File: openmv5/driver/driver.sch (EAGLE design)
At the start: 83 parts, among them IC1 TPS613222ADBVR, IC2 AP64060WU-7, IC3 LM321LVIDCKR, IC4 74LVC1G07GW,125, IC5 DRV8876RGTR, IC6 DRV8876RGTR, J1 OPENMV5-TOP, J2 1771088, Q1 BUK6D120-60PX, U1 74LVC1G17SE-7

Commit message: Finish up driver shield
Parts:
- C16, C17: value EEV226M050S9GAA -> EMZR500ARA101MF80G; device EEV226M050S9GAA:EEV226M050S9GAA -> EMZR500ARA101MF80G:EMZR500ARA101MF80G; MPN EEV226M050S9GAA -> EMZR500ARA101MF80G
- R10: MPN CRCW04021K00FKEDC -> AC0402FR-1310KL
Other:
- note added: "* PMODE States: ---Low--- (Speed/Direction Mode) P7 = PWM P7=0% -> Out1,Out2=L,L (motor break) P7=1%-100% (below) P0 = Direction P0=L -> Out1,Out2=L,H (motor reverse) P0=H -> Out1,Out2=H,L (motor forward) ---High--- (H-Bridge Mode - Can be PWMed) P0,P8=L,L -> Out1,Out2=Hi-Z,Hi-Z (motor coast) P0,P8=L,H -> Out1,Out2=H,L (motor forward) P0,P8=H,L -> Out1,Out2=L,H (motor reverse) P0,P8=H,H -> Out1,O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"
- note added: "* PMODE States: ---Low--- (Speed/Direction Mode) P8 = PWM P8=0% -> Out3,Out4=L,L (motor break) P8=1%-100% (below) P12 = Direction P12=L -> Out3,Out4=L,H (motor reverse) P12=H -> Out3,Out4=H,L (motor forward) ---High--- (H-Bridge Mode - Can be PWMed) P12,P8=L,L -> Out3,Out4=Hi-Z,Hi-Z (motor coast) P12,P8=L,H -> Out3,Out4=H,L (motor forward) P12,P8=H,L -> Out3,Out4=L,H (motor reverse) P12,P8=H,H ->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"
- moved on the sheet: C13, C15, C17, C20, C21, D11, D13, IC6, JP11, R13, R15

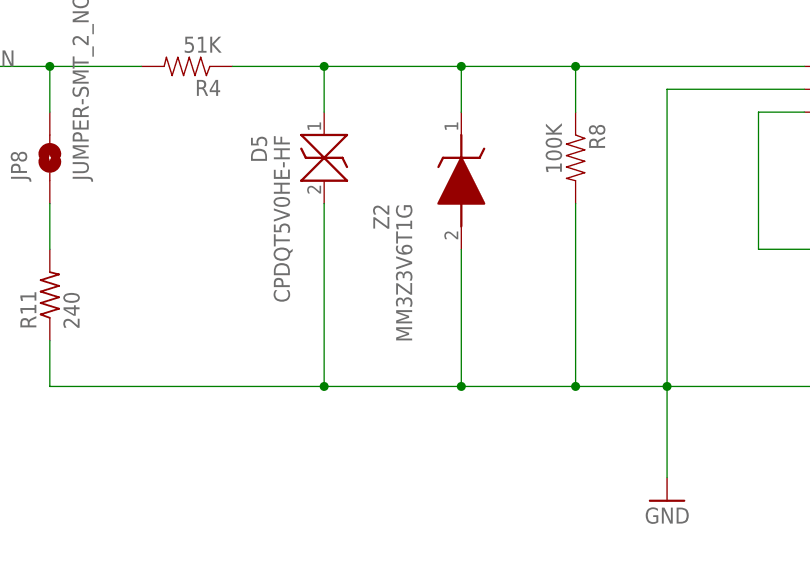
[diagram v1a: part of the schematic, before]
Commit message: Remove zener diode from ADC circuit
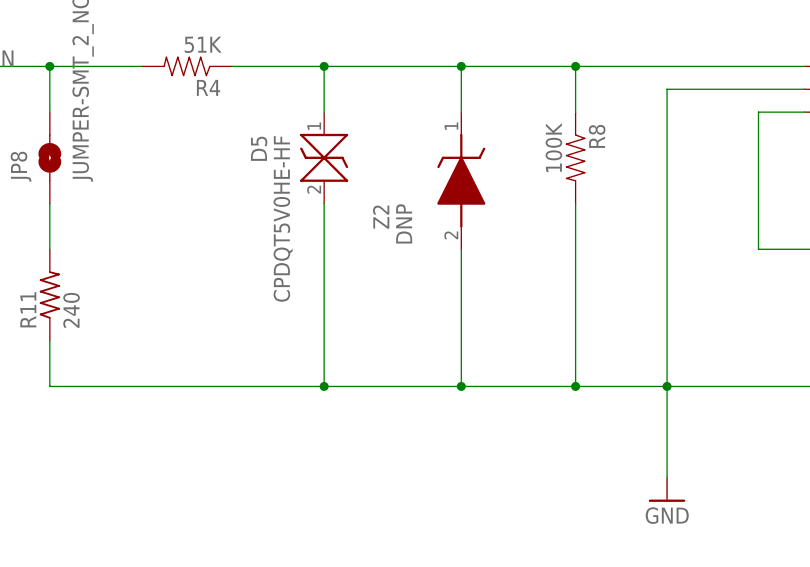
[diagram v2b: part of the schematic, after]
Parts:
- Z2: value MM3Z3V6T1G -> DNP; POPULATE (none) -> 0
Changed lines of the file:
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@@
 </part>
 <part name="GND7" library="sfe" deviceset="GND" device=""/>
-<part name="Z2" library="MM3Z3V6T1G" deviceset="MM3Z3V6T1G" device="">
+<part name="Z2" library="MM3Z3V6T1G" deviceset="MM3Z3V6T1G" device="" value="DNP">
 <attribute name="MPN" value="MM3Z3V6T1G"/>
+<attribute name="POPULATE" value="0"/>
 </part>
 <part name="R11" library="rcl" library_urn="urn:adsk.eagle:library:334" deviceset="R-US_" device="R0603" package3d_urn="urn:adsk.eagle:package:23555/3" value="240">
@@
 <attribute name="VALUE" x="308.61" y="233.68" size="1.778" layer="96" rot="MR270" align="center-left"/>
 <attribute name="MPN" x="314.96" y="243.84" size="1.778" layer="96" rot="MR270" display="off"/>
+<attribute name="POPULATE" x="314.96" y="243.84" size="1.778" layer="96" rot="MR270" display="off"/>
 </instance>
 <instance part="R11" gate="G$1" x="269.24" y="223.52" smashed="yes" rot="R90">

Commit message: Update boards
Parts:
- removed Z3: MMSZ5231B-7-F, MMSZ5231B-7-F:MMSZ5231B-7-F
- added D14: CPDQT5V0HE-HF, CPDQT5V0HE-HF:CPDQT5V0HE-HF
- D10: value CPDQT5V0HE-HF -> BAT54S_R1_00001; device CPDQT5V0HE-HF:CPDQT5V0HE-HF -> BAT54S_R1_00001:BAT54S_R1_00001; MPN CPDQT5V0HE-HF -> BAT54S_R1_00001
- Z2: value DNP -> MMSZ5231B-7-F; device MM3Z3V6T1G:MM3Z3V6T1G -> MMSZ5231B-7-F:MMSZ5231B-7-F; MPN MM3Z3V6T1G -> MMSZ5231B-7-F; POPULATE 0 -> (none)
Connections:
- net AIN_INT: now also D10.A/K; no longer Z2.K
- net GND: now also D10.A, D14.2; no longer D10.2, Z3.A
- net P0_PWM: now also D13.1; no longer D12.1
- net P12_PWM: now also D14.1; no longer D13.1
- net P7_PWM: now also D11.1; no longer D10.1
- net P8_PWM: now also D12.1; no longer D11.1
- net SYNC_IN_INT: now also Z2.K; no longer Z3.K
- net VCC: now also D10.K
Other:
- moved on the sheet: D10, D11, D12, D13, Z2
